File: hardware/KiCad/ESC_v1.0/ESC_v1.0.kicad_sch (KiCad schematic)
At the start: 39 parts, among them J3 USB4105-GF-A, J4 Conn_ARM_SWD_TagConnect_TC203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, U1 STM32G484CEU6, U2 LM5160A, U8 USBLC6-2SC6, X1 16MHz

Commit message: Kicad Update
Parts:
- removed C15: C, symbol Device:C
- removed R5, R6: R, symbol Device:R
- added C1: 700n, Capacitor_SMD:C_0603_1608Metric, symbol ESC-SchemSymLib:CL10A105KB8NNNC
- added C12, C13, C17, C18, C26, C27: 4.7u, Capacitor_SMD:C_0805_2012Metric, symbol ESC-SchemSymLib:CL21A475KAQNNNE
- added C14, C15, C16, C21: 22u, Capacitor_SMD:C_0805_2012Metric, symbol ESC-SchemSymLib:CL21A475KAQNNNE
- added C19, C28: 100n, Capacitor_SMD:C_0402_1005Metric, symbol ESC-SchemSymLib:CL05B104KO5NNNC
- added C20, C25, CIN: 1u, Capacitor_SMD:C_0603_1608Metric, symbol ESC-SchemSymLib:CL10A105KB8NNNC
- added C22: 10n, Capacitor_SMD:C_0402_1005Metric, symbol ESC-SchemSymLib:CL05B103KB5NNNC
- added C23, C24: 330u, symbol Device:C_Polarized
- added C29, C30, C31: 470p, Capacitor_SMD:C_0402_1005Metric, symbol ESC-SchemSymLib:CL05B103KB5NNNC
- added CBST2: 1u, symbol Device:C
- added D1, D2, D3: D, symbol Device:D
- added D4: D_TVS, symbol ESC-SchemSymLib:D_TVS
- added J1: Conn_01x03_Socket, symbol Connector:Conn_01x03_Socket
- added Q1, Q2: NVMFS5C604N, symbol ESC-SchemSymLib:NVMFS5C604NL
- added R10, R11, R9: 3.48k, symbol Device:R
- added R12, R13, R14: 43.2k, symbol Device:R
- added R15: 130k, symbol Device:R
- added R16, R3, R4, R6 (x2), RFB1: 10k, symbol Device:R
- added R2, R3, R4, R5: 10, symbol Device:R
- added R5: 1, symbol Device:R
- added R7: 5, symbol Device:R
- added R8: ~, symbol Device:R
- added RFB2: 39.2k, symbol Device:R
- added U3: TPS7B92033, symbol ESC-SchemSymLib:TPS7B92033
- added U4: 2EDL8024, symbol ESC-SchemSymLib:2EDL8024
- CBST: renamed from C13; value C -> 10n
- CVCC: renamed from C14; value C -> 1u
- L1: value L -> 18u 2.48A
- RON: renamed from R2; value R -> 110k
- RUV1: renamed from R4; value R -> 9.31k
- RUV2: renamed from R3; value R -> 124k
- renumbered C16 to CSS
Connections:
- net +10V: now also C17.1, C18.1, C19.1, C20.1, CBST2.1, R7.2, RFB2.1, U3.1 (VIN), U4.1 (VDD)
- net +3V3: now also C12.1, U3.5 (OUT)
- net AGND: now also R34.2, C12.2, C13.2, C14.2, C15.2, C16.2, C17.2, C18.2, C19.2, C20.2, C21.2, C22.2, C23.2, C24.2, C25.2, C26.2, C27.2, C28.2, C29.2, C30.2, C31.2, CBST2.2, CIN.2, D4.1 (A1), R12.2, R13.2, R14.2, R15.2, R3.2, R4.2, RFB1.2, U3.2 (GND), U3.3 (NC), U3.4 (NC), U4.7 (VSS), U4.PAD (VSS); no longer R34.1
- net PWM1: now also U4.5 (HI)
- net PWM1N: now also U4.6 (LI)
- net VBAT: now also D4.2 (A2), R8.1; no longer RON.1, RUV2.1, U2.3 (VIN)
- net +10VN: now reaches CBST.1, L1.1, U2.11 (SW), U2.12 (SW)
- net at U2.8 (FB): now also RFB1.1, RFB2.2
- net at J3.A5 (CC1): now also R34.1; no longer R34.2
- new net: C22.1, R5.2
- new net: Q1.2 (G), R2.1, R3.1, R6.1
- new net: D1.1 (K), R3.2, U4.3 (HO)
- new net: Q2.2 (G), R4.1, R4.1, R5.1
- new net: D3.2 (A), R7.1
- new net: D2.1 (K), R5.2, U4.8 (LO)
- new net: D2.2 (A), R4.2
- new net: D1.2 (A), R2.2
- new net: C1.1, D3.1 (K), U4.2 (HB)
- new net +VPH1: C1.2, Q1.3 (S), Q2.1 (D), R5.1, R6.2, U4.4 (HS)
- new net ISENSE1: Q2.3 (S), R3.1
- new net Long cul de sac trace: R15.1, R16.2
- new net PH1: J1.1 (Pin_1), R16.1, R9.1
- new net PH2: J1.2 (Pin_2), R10.1
- new net PH3: J1.3 (Pin_3), R11.1
- new net VABC: R6.1
- new net VM: C13.1, C14.1, C15.1, C16.1, C21.1, C23.1, C24.1, C25.1, C26.1, C27.1, C28.1, CIN.1, Q1.1 (D), R6.2, R8.2, RON.1, RUV2.1, U2.3 (VIN)
- new net VSENSE1: C31.1, R12.1, R9.2
- new net VSENSE2: C30.1, R10.2, R13.1
- new net VSENSE3: C29.1, R11.2, R14.1
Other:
- note added: "10V to 3V3 LDO"
- note added: "Compact divider"
- note added: "Must be placed near MCU ADC pins."
- note added: "PHASE A/B/C"
- note added: "VBAT FILTERING"
- note added: "VM to 10V BUCK"
- note added: "VOLTAGE SENSING A/B/C"
- note removed: "I_limit = 500/R_ILIM Here we set I_limit = 2A --------------- Sitching logic: VSNS = V_IN1 * R7/(R6+R7) if VSNS > 0.8V => OUT = IN1 otherwise take the highest input --------------- We want: if V_IN1 > 5V => OUT = IN1"
- moved on the sheet: C1, C10, C11, C2, C3, C4, C43, C44, C5, C6, C7, C8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

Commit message: Update on doc and kicad
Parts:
- removed C13, C17, C18, C26, C27: 4.7u, Capacitor_SMD:C_0805_2012Metric, symbol ESC-SchemSymLib:CL21A475KAQNNNE
- removed C19, C28: 100n, Capacitor_SMD:C_0402_1005Metric, symbol ESC-SchemSymLib:CL05B104KO5NNNC
- removed C25: 1u, Capacitor_SMD:C_0603_1608Metric, symbol ESC-SchemSymLib:CL10A105KB8NNNC
- removed CBST: 10n, symbol Device:C
- removed R15: 130k, symbol Device:R
- removed R4, R6 (x2): 10k, symbol Device:R
- removed R5: 1, symbol Device:R
- removed RFB2: 39.2k, symbol Device:R
- added C25, C26, C27: 10n, Capacitor_SMD:C_0402_1005Metric, symbol ESC-SchemSymLib:CL05B103KB5NNNC
- added C30: 4.7u, Capacitor_SMD:C_0805_2012Metric, symbol ESC-SchemSymLib:CL21A475KAQNNNE
- added C33: 1u, Capacitor_SMD:C_0603_1608Metric, symbol ESC-SchemSymLib:CL10A105KB8NNNC
- added C35: 100n, Capacitor_SMD:C_0402_1005Metric, symbol Device:C
- added D2, D3: PWR_LED, LED_SMD:LED_0603_1608Metric, symbol Device:LED
- added J1: Conn_01x03_Socket, symbol Connector:Conn_01x03_Socket
- added LED1: 19-337C/RSBHGHC-A88/4T, FC-FootprintLib:SMD-B_19-337C_EVE, symbol ESC-SchemSymLib:LED_19-337C
- added R10, R12, R9: 47, symbol Device:R
- added R11, R19, R36: 10k, Resistor_SMD:R_0603_1608Metric, symbol ESC-SchemSymLib:0603WAF1002T5E
- added R17, R18: 1, symbol Device:R
- added R21: 4.7k, symbol Device:R
- added R22: 1.5k, Resistor_SMD:R_0402_1005Metric, symbol Device:R
- added R26, R27, R28: 220, Resistor_SMD:R_0402_1005Metric, symbol Device:R
- added TP1, TP10, TP11, TP12, TP13, TP14, TP15, TP17, TP18, TP19, TP2, TP20, TP21, TP22, TP23, TP24, TP25, TP26, TP3, TP4, TP6, TP7, TP8, TP9: TestPoint, symbol Connector:TestPoint
- C20: renamed from CVCC; footprint (none) -> Capacitor_SMD:C_0402_1005Metric
- C21: renamed from C29; value 470p -> 100p
- C22: renamed from C30; value 470p -> 100p
- C23: renamed from C31; value 470p -> 100p
- C28: renamed from CBST2; footprint (none) -> Capacitor_SMD:C_0603_1608Metric
- Q1, Q2: footprint (none) -> Package_SO:ONSemi_SO-8FL_488AA
- R16: value 10k -> 1
- R20: renamed from RFB1; value 10k -> 39.2k
- R38: renamed from R3; value 10k -> 250u
- U2: footprint (none) -> Package_SON:WSON-12-1EP_4x4mm_P0.5mm_EP2.6x3mm_ThermalVias
- U3: footprint (none) -> Package_TO_SOT_SMD:SOT-23-5
- U4: footprint (none) -> Package_DFN_QFN:DFN-8-1EP_4x4mm_P0.8mm_EP2.5x3.6mm
- renumbered C4 to C1, C23 to C12, C24 to C13, C16 to C14, C21 to C15, C14 to C16, C15 to C17, CIN to C18, CSS to C19, C3 to C2, C22 to C24, C12 to C29, C2 to C3, C43 to C31, C20 to C32, C44 to C34, C1 to C36, C1 to C4, C7 to C5, C5 to C7, C9 to C8, C8 to C9, D4 to D1, D6 to D4, D3 to D5, D1 to D6, D2 to D7, J1 to J2, J4 to J3, J3 to J4, R9 to R13, R10 to R14, R11 to R15, R8 to R2, R31 to R23, R32 to R24, R33 to R25, R7 to R29, RUV2 to R3, R34 to R30, R35 to R31, R2 to R32, R3 to R33, R5 to R34, R4 to R35, RUV1 to R4, RON to R5, R12 to R6, R13 to R7, R14 to R8, TP4 to TP16, TP1 to TP5, U8 to U5
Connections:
- net +VPH1 is gone; now on net PH1: C36.2, Q1.3 (S), Q2.1 (D), U4.4 (HS)
- net Long cul de sac trace is gone; now on an unnamed net: R16.2
- net +10V: now also C30.1, C33.1, R19.1, R21.1, TP13.1, TP17.1
- net +3.3V: now also C35.1, LED1.2, LED1.4, LED1.6
- net +3V3: now also R22.2, TP1.1, TP14.1
- net +3V3A: now also TP2.1
- net +3V3REF: now also TP4.1
- net AGND: now also C26.2, C27.2, C30.2, C33.2, C35.2, D2.1 (K), D3.1 (K), R11.2, TP10.1, TP11.1, TP15.1, TP18.1, TP25.1, TP26.1, TP3.1; no longer C12.2, C13.2, C14.2, C15.2, C16.2, C17.2, D1.1 (A1)
- net PH1: now also R36.2, TP22.1
- net PH2: now also R17.1
- net PH3: now also R18.1
- net PWM1: now also TP19.1
- net PWM1N: now also TP20.1
- net VBAT: now also TP6.1
- net VM: now also TP7.1, TP9.1
- net VSENSE1: now also R12.1, TP12.1; no longer C23.1
- net VSENSE2: now also R10.1; no longer C22.1
- net VSENSE3: now also R9.1; no longer C21.1
- net at U1.9 (PA1): now also J1.2 (Pin_2)
- net at Q1.2 (G), R32.1, R33.1: now also R36.1
- net at U2.10 (BST): now also C25.2
- net at R20.1, U2.8 (FB): now also R19.2
- net at D6.1 (K), R33.2, U4.3 (HO): now also TP23.1
- net at Q2.2 (G), R34.1, R35.1: now also R11.1
- net at D7.1 (K), R34.2, U4.8 (LO): now also TP24.1
- net at C36.1, D5.1 (K), U4.2 (HB): now also TP21.1
- net +10VN renamed +10VNoise
- net +10VNoise: now also C25.1
- new net: C27.1, R18.2
- new net: D2.2 (A), R21.2
- new net: C26.1, R17.2
- new net: C22.1, R10.2
- new net: C21.1, R9.2
- new net: C23.1, R12.2
- new net: D3.2 (A), R22.1
- new net LED_B_K: LED1.5, R28.2
- new net LED_G_K: LED1.3, R27.2
- new net LED_R_K: LED1.1, R26.2
- new net MCU: J1.3 (Pin_3)
- new net PGND: C12.2, C13.2, C14.2, C15.2, C16.2, C17.2, D1.1 (A1), TP8.1
- new net RGB_LED_B: R28.1
- new net RGB_LED_G: R27.1
- new net RGB_LED_R: R26.1
- no-connect marks 2 -> 3
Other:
- note added: "PHASE 1"
- note added: "RGB LED"
- note added: "RGB LED TIM4 R = 65 : 296 (20mA : 5mA)"
- note removed: "Compact divider"
- note removed: "PHASE A/B/C"
- moved on the sheet: C1, C10, C11, C12, C13, C14, C15, C16, C17, C18, C19, C2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

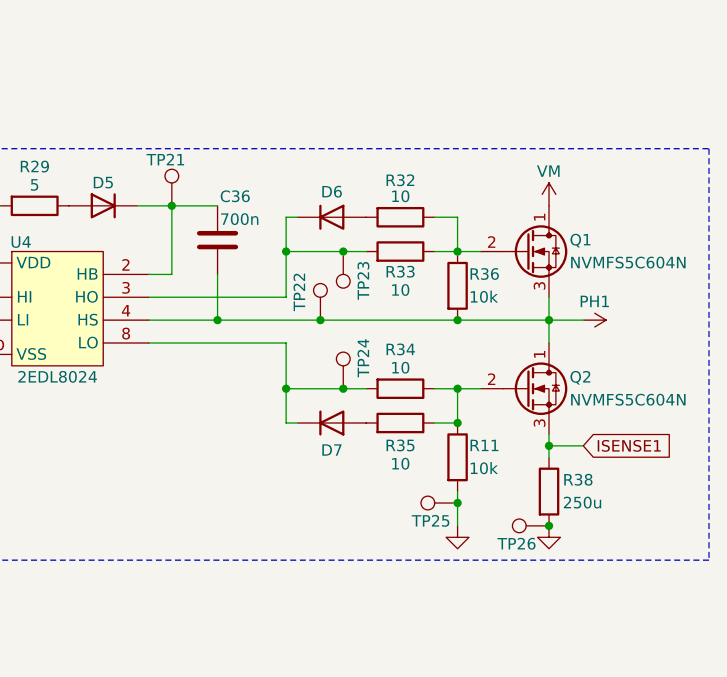
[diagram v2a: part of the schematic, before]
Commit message: Update gate driver
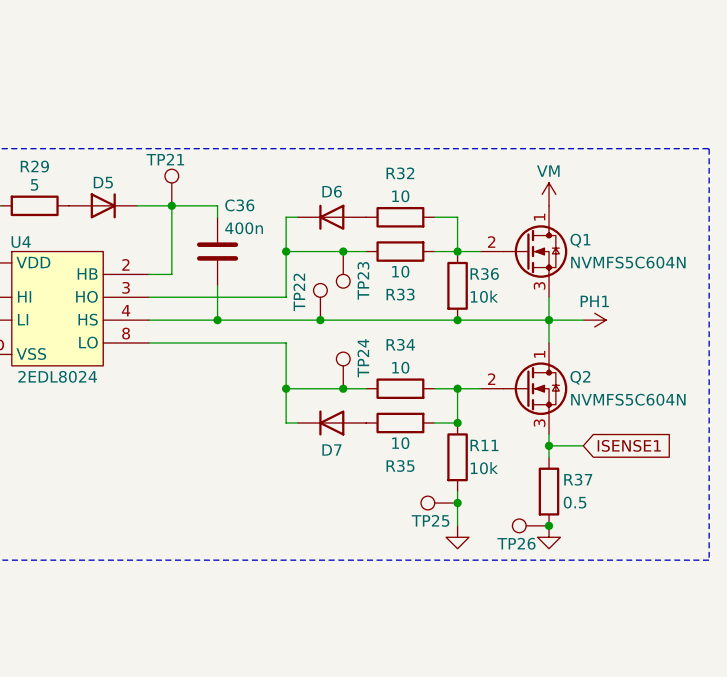
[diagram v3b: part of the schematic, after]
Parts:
- removed C36: 700n, Capacitor_SMD:C_0603_1608Metric, symbol ESC-SchemSymLib:CL10A105KB8NNNC
- removed R32, R33, R34, R35: 10, symbol Device:R
- removed R38: 250u, symbol Device:R
- added C36: 400n, symbol Device:C
- added R32, R33, R34, R35: 10, Resistor_SMD:R_0805_2012Metric, symbol ESC-SchemSymLib:0805W8F100JT5E
- added R37: 0.5, ESC-FootprintLib:Kelvin Shunt 1216 (3038), symbol ESC-SchemSymLib:HoBB1216-5W-0.5mR-1%
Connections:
- net AGND: now also R37.2
- net ISENSE1: now also R37.1
- net PH1: now also C36.2
- net at Q1.2 (G), R36.1: now also R32.2, R33.2
- net at D6.1 (K), TP23.1, U4.3 (HO): now also R33.1
- net at Q2.2 (G), R11.1: now also R34.2, R35.2
- net at D7.1 (K), TP24.1, U4.8 (LO): now also R34.1
- net at D7.2 (A): now also R35.1
- net at D6.2 (A): now also R32.1
- net at D5.1 (K), TP21.1, U4.2 (HB): now also C36.1

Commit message: Update doc and kicad
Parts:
- removed C21, C22, C23: 100p, Capacitor_SMD:C_0402_1005Metric, symbol ESC-SchemSymLib:CL05B103KB5NNNC
- removed C24, C26, C27: 10n, Capacitor_SMD:C_0402_1005Metric, symbol ESC-SchemSymLib:CL05B103KB5NNNC
- removed C30: 4.7u, Capacitor_SMD:C_0805_2012Metric, symbol ESC-SchemSymLib:CL21A475KAQNNNE
- removed C31: 1u, Capacitor_SMD:C_0402_1005Metric, symbol Device:C
- removed C34: 100n, Capacitor_SMD:C_0402_1005Metric, symbol Device:C
- removed C36: 400n, symbol Device:C
- removed D4: USB_LED, LED_SMD:LED_0603_1608Metric, symbol Device:LED
- removed D5, D6, D7: D, symbol Device:D
- removed F1: MF-MSMF050-2, Resistor_SMD:R_1812_4532Metric, symbol Device:Polyfuse
- removed J4: USB4105-GF-A, FC-FootprintLib:GCT_USB4105-GF-A, symbol FC-SchemSymbolLib:USB4105-GF-A
- removed R10, R12, R9: 47, symbol Device:R
- removed R13, R14, R15: 3.48k, symbol Device:R
- removed R16, R17, R18: 1, symbol Device:R
- removed R2: ~, symbol Device:R
- removed R23: 43k, Resistor_SMD:R_0402_1005Metric, symbol Device:R
- removed R24: 82k, Resistor_SMD:R_0402_1005Metric, symbol Device:R
- removed R25: 250, Resistor_SMD:R_0402_1005Metric, symbol Device:R
- removed R29: 5, symbol Device:R
- removed R30, R31: 5.1k, Resistor_SMD:R_0402_1005Metric, symbol Device:R
- removed R6, R7, R8: 43.2k, symbol Device:R
- removed TP16: TestPoint Pad, TestPoint:TestPoint_Pad_D1.0mm, symbol Connector:TestPoint
- removed TP6: TestPoint, symbol Connector:TestPoint
- removed U5: USBLC6-2SC6, Package_TO_SOT_SMD:SOT-23-6, symbol FC-SchemSymbolLib:USBLC6-2SC6
- added C21, C22, C23: 100p, Capacitor_SMD:C_0805_2012Metric, symbol ESC-SchemSymLib:CL10C101JB8NNNC
- added C36, C37, C38: 100n, Capacitor_SMD:C_0402_1005Metric, symbol ESC-SchemSymLib:CL05B104KO5NNNC
- added D5, D6, D7: RB161QS-40T18R, symbol ESC-SchemSymLib:RB161QS-40T18R
- added R10, R12, R9: 47, Resistor_SMD:R_0603_1608Metric, symbol ESC-SchemSymLib:0603WAF470JT5E
- added R13, R7, R8: 390, Resistor_SMD:R_0603_1608Metric, symbol ESC-SchemSymLib:0603WAF3900T5E
- added R14, R15, R6: 5.6k, Resistor_SMD:R_0603_1608Metric, symbol ESC-SchemSymLib:0603WAF5601T5E
- added R29: 5.1, Resistor_SMD:R_0805_2012Metric, symbol ESC-SchemSymLib:0805W8F510KT5E
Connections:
- net +10V: now also R29.1
- net AGND: now also C21.2, C22.2, C23.2, R14.1, R15.1, R6.1
- net PH1: now also R7.2
- net PH2: now also R8.2
- net PH3: now also R13.2
- net VSENSE1: now also R6.2, R7.1, R9.1
- net VSENSE2: now also R10.1, R14.2, R8.1
- net VSENSE3: now also R12.1, R13.1, R15.2
- net at TP21.1, U4.2 (HB): now also C36.1, C37.1, C38.1, D5.1 (K)
- net at R33.1, TP23.1, U4.3 (HO): now also C36.2, C37.2, C38.2, D6.1 (K)
- net at R34.1, TP24.1, U4.8 (LO): now also D7.1 (K)
- net at R35.1: now also D7.2 (A)
- net at R32.1: now also D6.2 (A)
- new net: C22.1, R10.2
- new net: D5.2 (A), R29.2
- new net: C21.1, R9.2
- new net: C23.1, R12.2
- no-connect marks 3 -> 1
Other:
- note removed: "CC1 and CC2 pulled down with 5.1k resistors => advertise USB devide mode --------- SBU1/2 for alternate DisplayPort mode --------- VBUS Sensing disabled"
- note removed: "USB-C"
- moved on the sheet: C32, C33, J2, TP17, TP18, TP19, TP20, TP21, U4

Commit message: Update kicad and docs
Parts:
- removed C20: 1u, Capacitor_SMD:C_0402_1005Metric, symbol Device:C
- removed C28: 1u, Capacitor_SMD:C_0603_1608Metric, symbol Device:C
- removed C35: 100n, Capacitor_SMD:C_0402_1005Metric, symbol Device:C
- removed D2, D3: PWR_LED, LED_SMD:LED_0603_1608Metric, symbol Device:LED
- removed R1: 82k, Resistor_SMD:R_0402_1005Metric, symbol Device:R
- removed R14: 5.6k, Resistor_SMD:R_0603_1608Metric, symbol ESC-SchemSymLib:0603WAF5601T5E
- removed R20: 39.2k, symbol Device:R
- removed R21: 4.7k, symbol Device:R
- removed R22: 1.5k, Resistor_SMD:R_0402_1005Metric, symbol Device:R
- removed R26, R27, R28: 220, Resistor_SMD:R_0402_1005Metric, symbol Device:R
- removed R3: 124k, symbol Device:R
- removed R4: 9.31k, symbol Device:R
- removed R5: 110k, symbol Device:R
- removed R7: 390, Resistor_SMD:R_0603_1608Metric, symbol ESC-SchemSymLib:0603WAF3900T5E
- added C20, C26, C27, C34, C35: 1u, Capacitor_SMD:C_0603_1608Metric, symbol ESC-SchemSymLib:CL10A105KB8NNNC
- added C24, C28, C30, C31, C39, C40, C41: 100n, Capacitor_SMD:C_0402_1005Metric, symbol ESC-SchemSymLib:CL05B104KO5NNNC
- added D10, D11, D12, D4, D8, D9: RB161QS-40T18R, symbol ESC-SchemSymLib:RB161QS-40T18R
- added D2, D3: KT-0603W, LED_SMD:LED_0603_1608Metric, symbol ESC-SchemSymLib:KT-0603W
- added Q3, Q4, Q5, Q6: NVMFS5C604N, Package_SO:ONSemi_SO-8FL_488AA, symbol ESC-SchemSymLib:NVMFS5C604NL
- added R1, R31: 5.1, Resistor_SMD:R_0805_2012Metric, symbol ESC-SchemSymLib:0805W8F510KT5E
- added R14, R2: 390, Resistor_SMD:R_0603_1608Metric, symbol ESC-SchemSymLib:0603WAF3900T5E
- added R16, R17, R18: 150, Resistor_SMD:R_0603_1608Metric, symbol ESC-SchemSymLib:0603WAF1500T5E
- added R20: 39k, Resistor_SMD:R_0603_1608Metric, symbol ESC-SchemSymLib:0603WAF3902T5E
- added R21: 1k, Resistor_SMD:R_0603_1608Metric, symbol ESC-SchemSymLib:0603WAF1001T5E
- added R22, R5: 120k, Resistor_SMD:R_0603_1608Metric, symbol ESC-SchemSymLib:0603WAF1203T5E
- added R23, R24, R25, R26, R38, R39, R40, R41: 10, Resistor_SMD:R_0805_2012Metric, symbol ESC-SchemSymLib:0805W8F100JT5E
- added R27, R28, R42, R43: 10k, Resistor_SMD:R_0603_1608Metric, symbol ESC-SchemSymLib:0603WAF1002T5E
- added R3: 22k, Resistor_SMD:R_0603_1608Metric, symbol ESC-SchemSymLib:0402WGF2202TCE
- added R30, R44: 0.5, ESC-FootprintLib:Kelvin Shunt 1216 (3038), symbol ESC-SchemSymLib:HoBB1216-5W-0.5mR-1%
- added R4: 200k, Resistor_SMD:R_0603_1608Metric, symbol ESC-SchemSymLib:0603WAF2003T5E
- added R7: 5.6k, Resistor_SMD:R_0603_1608Metric, symbol ESC-SchemSymLib:0603WAF5601T5E
- added TP16, TP27, TP28, TP29, TP30, TP31, TP32, TP33, TP34, TP35, TP36, TP37, TP38, TP39, TP40, TP41, TP42, TP43, TP44, TP6: TestPoint, symbol Connector:TestPoint
- added U5, U6: 2EDL8024, Package_DFN_QFN:DFN-8-1EP_4x4mm_P0.8mm_EP2.5x3.6mm, symbol ESC-SchemSymLib:2EDL8024
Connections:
- net +10V: now also C18.1, C26.1, C27.1, C34.1, C35.1, R1.1, R20.1, R21.1, R31.1, TP35.1, TP6.1, U5.1 (VDD), U6.1 (VDD); no longer R19.1
- net +3.3V: now also C24.1
- net +3V3: now also R16.1
- net AGND: now also R13.2, R19.2, R8.2, C20.2, C24.2, C26.2, C27.2, C34.2, C35.2, D2.1 (K), D3.1 (K), R14.2, R22.2, R28.2, R3.2, R30.2, R43.2, R44.2, TP16.1, TP33.1, TP34.1, TP36.1, TP43.1, TP44.1, U5.7 (VSS), U5.PAD (VSS), U6.7 (VSS), U6.PAD (VSS); no longer R15.1, R6.1
- net BOOT0: now also R22.1
- net ISENSE1: now also Q4.3 (S), Q6.3 (S), R30.1, R44.1
- net LED_B_K: now also R18.2
- net LED_G_K: now also R17.2
- net LED_R_K: now also R2.2
- net PH1: now also Q3.3 (S), Q4.1 (D), Q5.3 (S), Q6.1 (D), R27.2, R42.2, R7.1, TP30.1, TP40.1, U5.4 (HS), U6.4 (HS)
- net PH2: now also R6.1; no longer R8.2
- net PH3: now also R15.1; no longer R13.2
- net PWM1: now also TP27.1, TP37.1, U5.5 (HI), U6.5 (HI)
- net PWM1N: now also TP28.1, TP38.1, U5.6 (LI), U6.6 (LI)
- net RGB_LED_B: now also R18.1
- net RGB_LED_G: now also R17.1
- net RGB_LED_R: now also R2.1
- net VM: now also Q3.1 (D), Q5.1 (D), R4.1, R5.1; no longer C18.1
- net VSENSE1: now also R14.1, R7.2; no longer R6.2
- net VSENSE2: now also R13.1, R6.2; no longer R8.1
- net VSENSE3: now also R8.1; no longer R13.1
- net at U2.4 (EN/UVLO): now also R3.1, R4.2
- net at U2.5 (RON): now also R5.2
- net at U2.7 (FPWM), U2.9 (VCC): now also C20.1
- net at U2.8 (FB): now also R19.1, R20.2; no longer R19.2
- new net: D2.2 (A), R21.2
- new net: D12.1 (K), R40.1, TP42.1, U6.8 (LO)
- new net: Q4.2 (G), R25.2, R26.2, R28.1
- new net: C39.1, C40.1, C41.1, D10.1 (K), TP39.1, U6.2 (HB)
- new net: C39.2, C40.2, C41.2, D11.1 (K), R39.1, TP41.1, U6.3 (HO)
- new net: C28.1, C30.1, C31.1, D4.1 (K), TP29.1, U5.2 (HB)
- new net: D4.2 (A), R1.2
- new net: D12.2 (A), R41.1
- new net: D8.2 (A), R23.1
- new net: Q3.2 (G), R23.2, R24.2, R27.1
- new net: C28.2, C30.2, C31.2, D8.1 (K), R24.1, TP31.1, U5.3 (HO)
- new net: D9.1 (K), R25.1, TP32.1, U5.8 (LO)
- new net: Q6.2 (G), R40.2, R41.2, R43.1
- new net: D11.2 (A), R38.1
- new net: Q5.2 (G), R38.2, R39.2, R42.1
- new net: D3.2 (A), R16.2
- new net: D10.2 (A), R31.2
- new net: D9.2 (A), R26.1
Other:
- moved on the sheet: C1, C10, C11, C19, C2, C21, C22, C23, C25, C29, C3, C32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
